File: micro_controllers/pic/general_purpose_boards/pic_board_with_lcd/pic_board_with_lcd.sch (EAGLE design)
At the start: 29 parts, among them IC1 PIC16f877a, IC2 7805TV

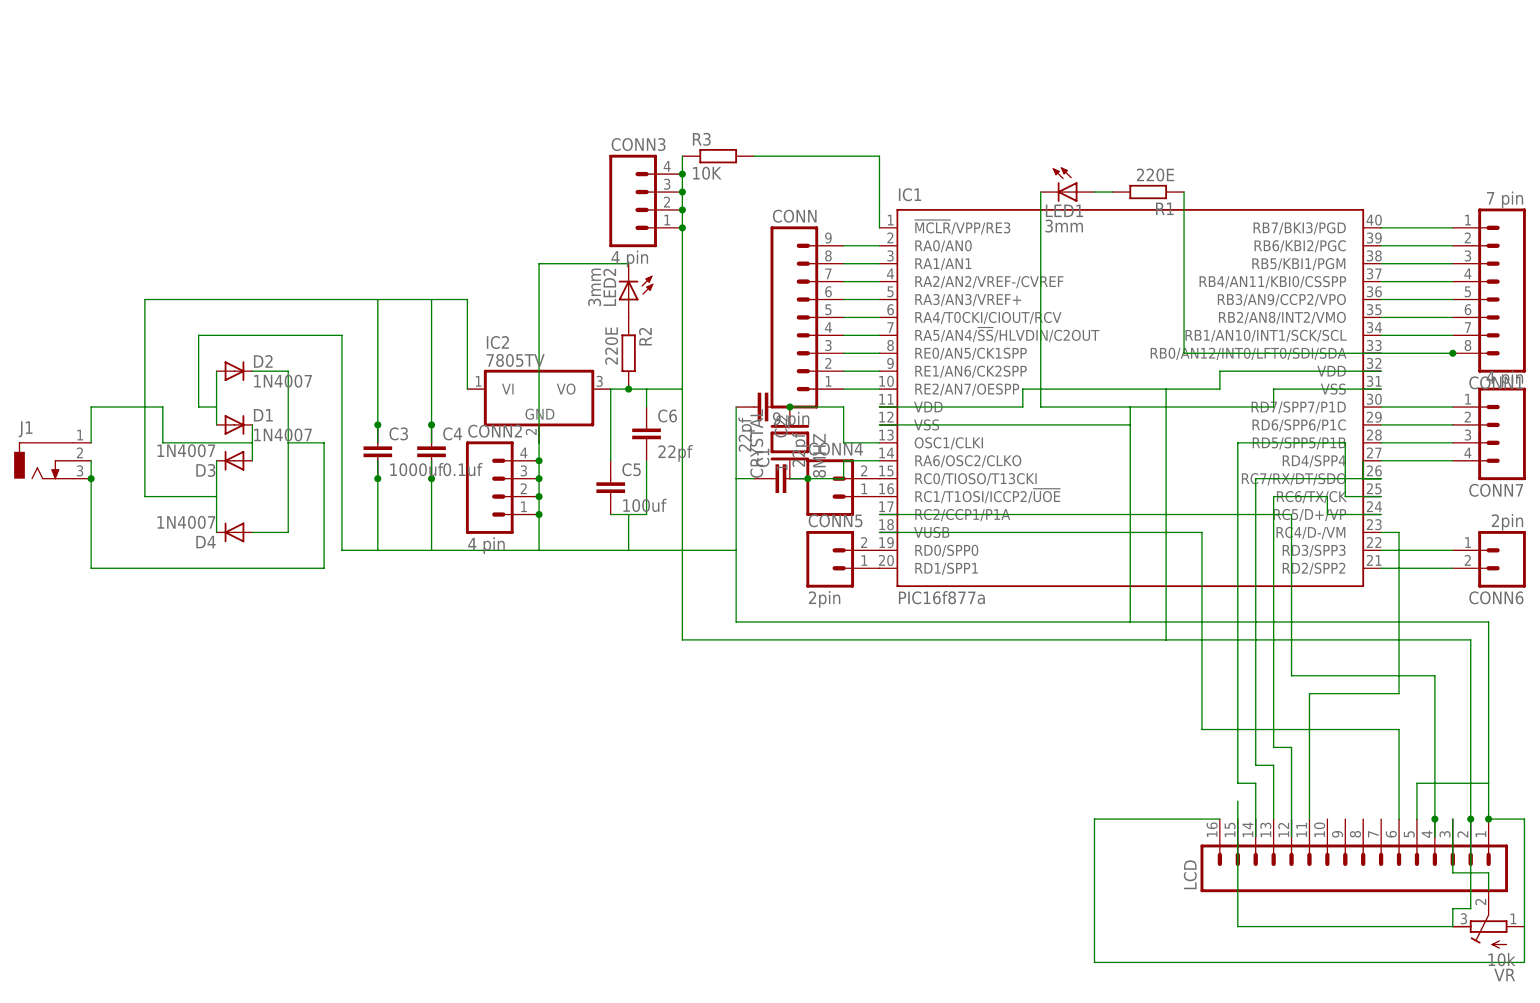
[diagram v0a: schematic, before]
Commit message: 
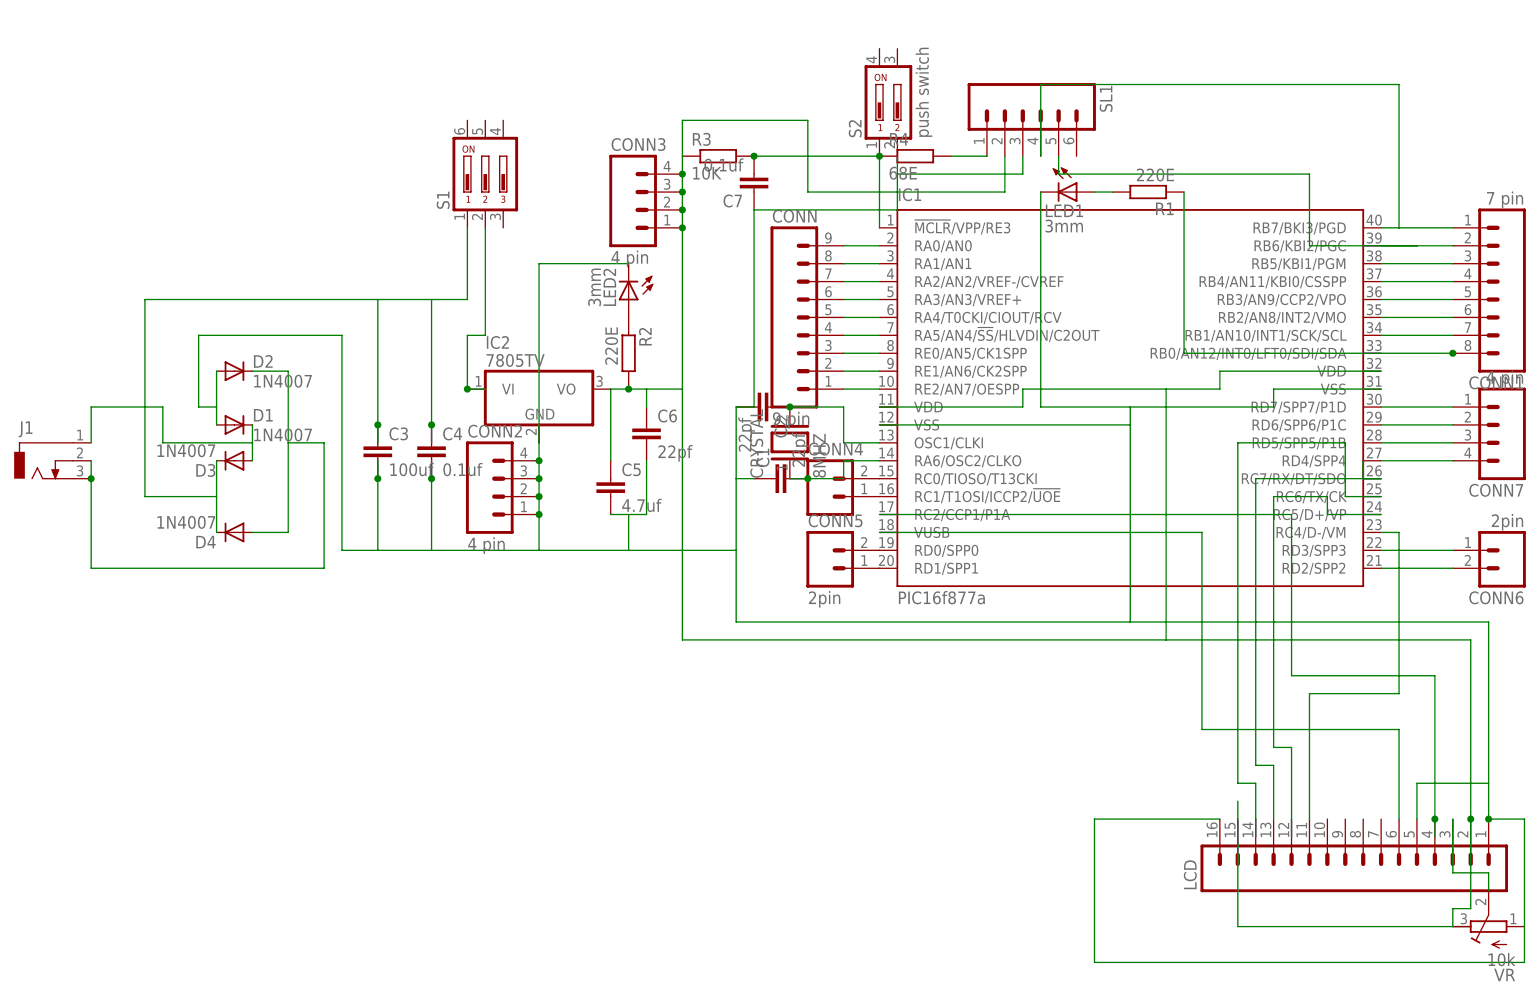
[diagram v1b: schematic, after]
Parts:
- added C7: 0.1uf, capacitor-wima:C2,5-3
- added R4: 68E, rcl:R-EU_0204/7
- added S1: (no value), switch-dil:DA03
- added S2: push switch, switch-dil:DP02
- added SL1: (no value), con-amp-quick:M06
- C3: value 1000uf -> 100uf
- C5: value 100uf -> 4.7uf
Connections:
- new net N$44: IC2.VI, S1.2
- new net N$45: R4.2, SL1.1
- net N$19: now also SL1.4
- net N$20: now also SL1.5
- net N$30: now also S1.1; no longer IC2.VI
- net N$33: now also SL1.2
- net N$35: now also C7.1, S2.2, SL1.3
- net N$39: now also C7.2, R4.1, S2.1
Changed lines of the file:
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@@
 <part name="D3" library="diode" deviceset="1N4004" device="" value="1N4007"/>
 <part name="D4" library="diode" deviceset="1N4004" device="" value="1N4007"/>
-<part name="C3" library="capacitor-wima" deviceset="C" device="5/7.2" value="1000uf"/>
+<part name="C3" library="capacitor-wima" deviceset="C" device="5/7.2" value="100uf"/>
 <part name="C4" library="capacitor-wima" deviceset="C" device="2,5-3" value="0.1uf"/>
 <part name="J1" library="con-jack" deviceset="DCJ0303" device=""/>
 <part name="IC2" library="linear" deviceset="78*" device="TV" technology="05"/>
-<part name="C5" library="capacitor-wima" deviceset="C" device="5/7.2" value="100uf"/>
+<part name="C5" library="capacitor-wima" deviceset="C" device="5/7.2" value="4.7uf"/>
 <part name="C6" library="capacitor-wima" deviceset="C" device="2.5/2" value="22pf"/>
 <part name="R1" library="rcl" deviceset="R-EU_" device="0204/7" value="220E"/>
@@
 <attribute name="OC_NEWARK" value="unknown"/>
 </part>
+<part name="S2" library="switch-dil" deviceset="DP02" device="" value="push switch"/>
+<part name="C7" library="capacitor-wima" deviceset="C" device="2,5-3" value="0.1uf"/>
+<part name="S1" library="switch-dil" deviceset="DA03" device=""/>
+<part name="SL1" library="con-amp-quick" deviceset="M06" device=""/>
+<part name="R4" library="rcl" deviceset="R-EU_" device="0204/7" value="68E"/>
 </parts>
 <sheets>
@@
 <instance part="CONN6" gate="G$1" x="134.62" y="38.1" rot="R180"/>
 <instance part="CONN7" gate="G$1" x="132.08" y="55.88" rot="R180"/>
+<instance part="S2" gate="1" x="45.72" y="101.6"/>
+<instance part="C7" gate="G$1" x="27.94" y="88.9" rot="R180"/>
+<instance part="S1" gate="1" x="-10.16" y="91.44"/>
+<instance part="SL1" gate="G$1" x="66.04" y="99.06" rot="R270"/>
+<instance part="R4" gate="G$1" x="50.8" y="93.98"/>
 </instances>
 <busses>
@@
 <pinref part="IC1" gate="G$1" pin="RB7/BKI3/PGD"/>
 <pinref part="CONN1" gate="G$1" pin="1"/>
-<wire x1="127" y1="83.82" x2="116.84" y2="83.82" width="0.1524" layer="91"/>
+<wire x1="127" y1="83.82" x2="119.38" y2="83.82" width="0.1524" layer="91"/>
+<pinref part="SL1" gate="G$1" pin="4"/>
+<wire x1="119.38" y1="83.82" x2="116.84" y2="83.82" width="0.1524" layer="91"/>
+<wire x1="68.58" y1="93.98" x2="68.58" y2="104.14" width="0.1524" layer="91"/>
+<wire x1="68.58" y1="104.14" x2="119.38" y2="104.14" width="0.1524" layer="91"/>
+<wire x1="119.38" y1="104.14" x2="119.38" y2="83.82" width="0.1524" layer="91"/>
 </segment>
 </net>
@@
 <pinref part="IC1" gate="G$1" pin="RB6/KBI2/PGC"/>
 <pinref part="CONN1" gate="G$1" pin="2"/>
-<wire x1="127" y1="81.28" x2="116.84" y2="81.28" width="0.1524" layer="91"/>
+<wire x1="127" y1="81.28" x2="121.92" y2="81.28" width="0.1524" layer="91"/>
+<pinref part="SL1" gate="G$1" pin="5"/>
+<wire x1="121.92" y1="81.28" x2="116.84" y2="81.28" width="0.1524" layer="91"/>
+<wire x1="71.12" y1="93.98" x2="71.12" y2="91.44" width="0.1524" layer="91"/>
+<wire x1="71.12" y1="91.44" x2="106.68" y2="91.44" width="0.1524" layer="91"/>
+<wire x1="106.68" y1="91.44" x2="106.68" y2="81.28" width="0.1524" layer="91"/>
+<wire x1="106.68" y1="81.28" x2="121.92" y2="81.28" width="0.1524" layer="91"/>
 </segment>
 </net>
@@
 <pinref part="C3" gate="G$1" pin="1"/>
 <junction x="-25.4" y="55.88"/>
-<pinref part="IC2" gate="A1" pin="VI"/>
-<wire x1="-12.7" y1="73.66" x2="-12.7" y2="60.96" width="0.1524" layer="91"/>
+<pinref part="S1" gate="1" pin="1"/>
+<wire x1="-12.7" y1="73.66" x2="-12.7" y2="83.82" width="0.1524" layer="91"/>
 </segment>
 </net>
@@
 <wire x1="96.52" y1="0" x2="96.52" y2="-15.24" width="0.1524" layer="91"/>
 <wire x1="96.52" y1="-15.24" x2="127" y2="-15.24" width="0.1524" layer="91"/>
+<pinref part="SL1" gate="G$1" pin="2"/>
+<wire x1="63.5" y1="93.98" x2="63.5" y2="88.9" width="0.1524" layer="91"/>
+<wire x1="63.5" y1="88.9" x2="35.56" y2="88.9" width="0.1524" layer="91"/>
+<wire x1="35.56" y1="88.9" x2="35.56" y2="99.06" width="0.1524" layer="91"/>
+<wire x1="35.56" y1="99.06" x2="17.78" y2="99.06" width="0.1524" layer="91"/>
+<wire x1="17.78" y1="99.06" x2="17.78" y2="93.98" width="0.1524" layer="91"/>
 </segment>
 </net>
@@
 <wire x1="76.2" y1="-20.32" x2="137.16" y2="-20.32" width="0.1524" layer="91"/>
 <wire x1="137.16" y1="-20.32" x2="137.16" y2="-15.24" width="0.1524" layer="91"/>
+<pinref part="C7" gate="G$1" pin="1"/>
+<wire x1="25.4" y1="58.42" x2="27.94" y2="58.42" width="0.1524" layer="91"/>
+<wire x1="27.94" y1="58.42" x2="27.94" y2="86.36" width="0.1524" layer="91"/>
+<pinref part="S2" gate="1" pin="2"/>
+<wire x1="27.94" y1="86.36" x2="48.26" y2="86.36" width="0.1524" layer="91"/>
+<wire x1="48.26" y1="86.36" x2="48.26" y2="91.44" width="0.1524" layer="91"/>
+<pinref part="SL1" gate="G$1" pin="3"/>
+<wire x1="48.26" y1="91.44" x2="48.26" y2="93.98" width="0.1524" layer="91"/>
+<wire x1="66.04" y1="93.98" x2="66.04" y2="91.44" width="0.1524" layer="91"/>
+<wire x1="66.04" y1="91.44" x2="48.26" y2="91.44" width="0.1524" layer="91"/>
 </segment>
 </net>
@@
 <wire x1="45.72" y1="93.98" x2="27.94" y2="93.98" width="0.1524" layer="91"/>
 <pinref part="R3" gate="G$1" pin="2"/>
+<pinref part="S2" gate="1" pin="1"/>
+<junction x="45.72" y="93.98"/>
+<pinref part="C7" gate="G$1" pin="2"/>
+<junction x="27.94" y="93.98"/>
+<pinref part="R4" gate="G$1" pin="1"/>
 </segment>
 </net>
@@
 </segment>
 </net>
+<net name="N$44" class="0">
+<segment>
+<wire x1="-10.16" y1="60.96" x2="-12.7" y2="60.96" width="0.1524" layer="91"/>
+<wire x1="-12.7" y1="60.96" x2="-12.7" y2="68.58" width="0.1524" layer="91"/>
+<pinref part="S1" gate="1" pin="2"/>
+<wire x1="-12.7" y1="68.58" x2="-10.16" y2="68.58" width="0.1524" layer="91"/>
+<wire x1="-10.16" y1="68.58" x2="-10.16" y2="83.82" width="0.1524" layer="91"/>
+<pinref part="IC2" gate="A1" pin="VI"/>
+<junction x="-12.7" y="60.96"/>
+</segment>
+</net>
+<net name="N$45" class="0">
+<segment>
+<pinref part="R4" gate="G$1" pin="2"/>
+<pinref part="SL1" gate="G$1" pin="1"/>
+<wire x1="55.88" y1="93.98" x2="60.96" y2="93.98" width="0.1524" layer="91"/>
+</segment>
+</net>

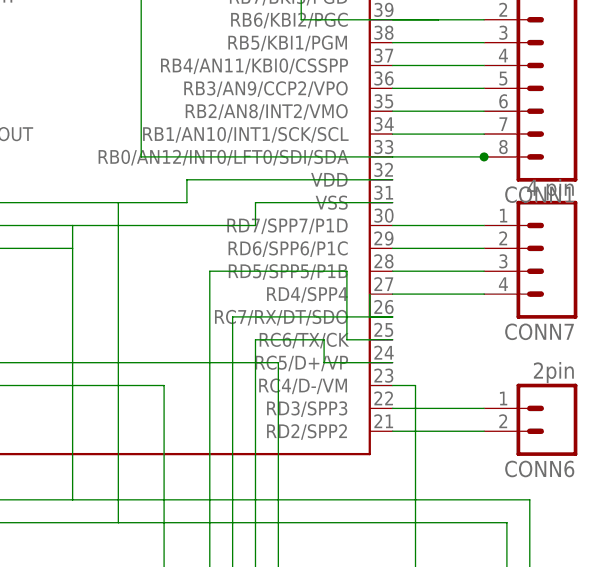
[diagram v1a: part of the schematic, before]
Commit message: 
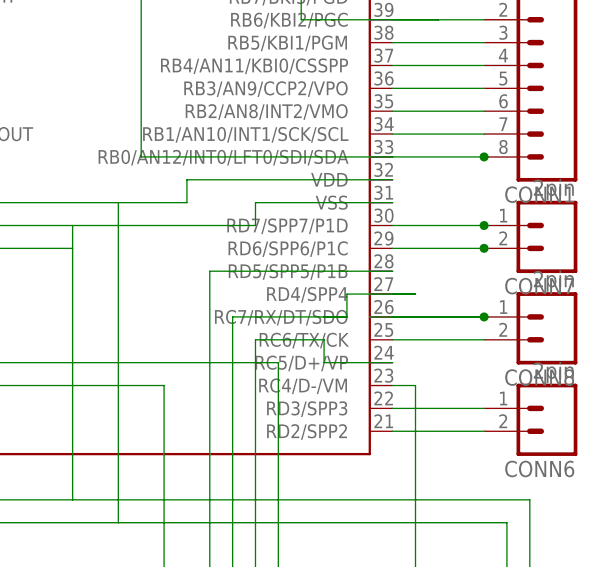
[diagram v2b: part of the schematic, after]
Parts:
- added CONN8: 2pin, con-amp-quick:M02
- CONN7: value 4 pin -> 2pin; device con-amp-quick:M04 -> con-amp-quick:M02
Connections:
- removed net N$37: CONN7.4, IC1.RD4/SPP4
- new net N$48: CONN8.1, IC1.RC7/RX/DT/SDO
- net N$36: now also CONN8.2, IC1.RC6/TX/CK; no longer CONN7.3, IC1.RD5/SPP5/P1B
- net N$42: now also IC1.RD4/SPP4; no longer IC1.RC6/TX/CK
- net N$43: now also IC1.RD5/SPP5/P1B; no longer IC1.RC7/RX/DT/SDO
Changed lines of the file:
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@@
 <part name="CONN4" library="con-amp-quick" deviceset="M02" device=""/>
 <part name="CONN6" library="con-amp-quick" deviceset="M02" device="" value="2pin"/>
-<part name="CONN7" library="con-amp-quick" deviceset="M04" device="" value="4 pin">
+<part name="S2" library="switch-dil" deviceset="DP02" device="" value="push switch"/>
+<part name="C7" library="capacitor-wima" deviceset="C" device="2,5-3" value="0.1uf"/>
+<part name="S1" library="switch-dil" deviceset="DA03" device=""/>
+<part name="SL1" library="con-amp-quick" deviceset="M06" device=""/>
+<part name="R4" library="rcl" deviceset="R-EU_" device="0204/7" value="68E"/>
+<part name="CONN7" library="con-amp-quick" deviceset="M02" device="" value="2pin">
 <attribute name="MF" value=""/>
 <attribute name="MPN" value=""/>
@@
 <attribute name="OC_NEWARK" value="unknown"/>
 </part>
-<part name="S2" library="switch-dil" deviceset="DP02" device="" value="push switch"/>
-<part name="C7" library="capacitor-wima" deviceset="C" device="2,5-3" value="0.1uf"/>
-<part name="S1" library="switch-dil" deviceset="DA03" device=""/>
-<part name="SL1" library="con-amp-quick" deviceset="M06" device=""/>
-<part name="R4" library="rcl" deviceset="R-EU_" device="0204/7" value="68E"/>
+<part name="CONN8" library="con-amp-quick" deviceset="M02" device="" value="2pin">
+<attribute name="MF" value=""/>
+<attribute name="MPN" value=""/>
+<attribute name="OC_FARNELL" value="unknown"/>
+<attribute name="OC_NEWARK" value="unknown"/>
+</part>
 </parts>
 <sheets>
@@
 <instance part="CONN4" gate="G$1" x="38.1" y="45.72"/>
 <instance part="CONN6" gate="G$1" x="134.62" y="38.1" rot="R180"/>
-<instance part="CONN7" gate="G$1" x="132.08" y="55.88" rot="R180"/>
 <instance part="S2" gate="1" x="45.72" y="101.6"/>
 <instance part="C7" gate="G$1" x="27.94" y="88.9" rot="R180"/>
@@
 <instance part="SL1" gate="G$1" x="66.04" y="99.06" rot="R270"/>
 <instance part="R4" gate="G$1" x="50.8" y="93.98"/>
+<instance part="CONN7" gate="G$1" x="134.62" y="58.42" rot="R180"/>
+<instance part="CONN8" gate="G$1" x="134.62" y="48.26" rot="R180"/>
 </instances>
 <busses>
@@
 <pinref part="CONN7" gate="G$1" pin="1"/>
 <wire x1="127" y1="58.42" x2="116.84" y2="58.42" width="0.1524" layer="91"/>
+<junction x="127" y="58.42"/>
 </segment>
 </net>
@@
 <pinref part="CONN7" gate="G$1" pin="2"/>
 <wire x1="127" y1="55.88" x2="116.84" y2="55.88" width="0.1524" layer="91"/>
-</segment>
-</net>
-<net name="N$36" class="0">
-<segment>
-<pinref part="IC1" gate="G$1" pin="RD5/SPP5/P1B"/>
-<pinref part="CONN7" gate="G$1" pin="3"/>
-<wire x1="127" y1="53.34" x2="116.84" y2="53.34" width="0.1524" layer="91"/>
-</segment>
-</net>
-<net name="N$37" class="0">
-<segment>
-<pinref part="IC1" gate="G$1" pin="RD4/SPP4"/>
-<pinref part="CONN7" gate="G$1" pin="4"/>
-<wire x1="127" y1="50.8" x2="116.84" y2="50.8" width="0.1524" layer="91"/>
+<junction x="127" y="55.88"/>
 </segment>
 </net>
@@
 <net name="N$42" class="0">
 <segment>
-<pinref part="IC1" gate="G$1" pin="RC6/TX/CK"/>
-<wire x1="116.84" y1="45.72" x2="111.76" y2="45.72" width="0.1524" layer="91"/>
-<wire x1="111.76" y1="45.72" x2="111.76" y2="48.26" width="0.1524" layer="91"/>
-<wire x1="111.76" y1="48.26" x2="99.06" y2="48.26" width="0.1524" layer="91"/>
+<wire x1="111.76" y1="48.26" x2="109.22" y2="48.26" width="0.1524" layer="91"/>
+<wire x1="109.22" y1="48.26" x2="99.06" y2="48.26" width="0.1524" layer="91"/>
 <wire x1="99.06" y1="48.26" x2="99.06" y2="7.62" width="0.1524" layer="91"/>
 <pinref part="LCD" gate="G$1" pin="13"/>
 <wire x1="99.06" y1="7.62" x2="101.6" y2="7.62" width="0.1524" layer="91"/>
 <wire x1="101.6" y1="7.62" x2="101.6" y2="0" width="0.1524" layer="91"/>
+<wire x1="109.22" y1="48.26" x2="111.76" y2="48.26" width="0.1524" layer="91"/>
+<wire x1="111.76" y1="48.26" x2="111.76" y2="50.8" width="0.1524" layer="91"/>
+<pinref part="IC1" gate="G$1" pin="RD4/SPP4"/>
+<wire x1="119.38" y1="50.8" x2="116.84" y2="50.8" width="0.1524" layer="91"/>
+<wire x1="111.76" y1="50.8" x2="119.38" y2="50.8" width="0.1524" layer="91"/>
 </segment>
 </net>
 <net name="N$43" class="0">
 <segment>
-<pinref part="IC1" gate="G$1" pin="RC7/RX/DT/SDO"/>
-<wire x1="116.84" y1="48.26" x2="114.3" y2="48.26" width="0.1524" layer="91"/>
-<wire x1="114.3" y1="48.26" x2="114.3" y2="50.8" width="0.1524" layer="91"/>
-<wire x1="116.84" y1="48.26" x2="111.76" y2="48.26" width="0.1524" layer="91"/>
-<wire x1="111.76" y1="48.26" x2="111.76" y2="53.34" width="0.1524" layer="91"/>
 <wire x1="111.76" y1="53.34" x2="96.52" y2="53.34" width="0.1524" layer="91"/>
 <wire x1="96.52" y1="53.34" x2="96.52" y2="5.08" width="0.1524" layer="91"/>
@@
 <wire x1="99.06" y1="5.08" x2="99.06" y2="0" width="0.1524" layer="91"/>
 <wire x1="99.06" y1="0" x2="99.06" y2="-2.54" width="0.1524" layer="91"/>
+<pinref part="IC1" gate="G$1" pin="RD5/SPP5/P1B"/>
+<wire x1="111.76" y1="53.34" x2="116.84" y2="53.34" width="0.1524" layer="91"/>
 </segment>
 </net>
@@
 </segment>
 </net>
+<net name="N$48" class="0">
+<segment>
+<pinref part="IC1" gate="G$1" pin="RC7/RX/DT/SDO"/>
+<wire x1="127" y1="48.26" x2="114.3" y2="48.26" width="0.1524" layer="91"/>
+<pinref part="CONN8" gate="G$1" pin="1"/>
+<junction x="127" y="48.26"/>
+<wire x1="127" y1="48.26" x2="116.84" y2="48.26" width="0.1524" layer="91"/>
+</segment>
+</net>
+<net name="N$36" class="0">
+<segment>
+<pinref part="IC1" gate="G$1" pin="RC6/TX/CK"/>
+<pinref part="CONN8" gate="G$1" pin="2"/>
+<wire x1="127" y1="45.72" x2="116.84" y2="45.72" width="0.1524" layer="91"/>
+</segment>
+</net>
